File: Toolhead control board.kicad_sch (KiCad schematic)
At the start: 28 parts, among them J1 Conn_01x02_Pin, J2 Conn_01x02_Pin, J3 Conn_01x06_Pin, J4 Conn_01x02_Pin, J5 Conn_01x02_Pin, J6 Conn_01x02_Pin, Q1 AS3400, Q2 AS3400, Q3 AS3400, U1 ADXL345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

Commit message: Rev1. Uart interface
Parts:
- removed J3: Conn_01x06_Pin, Connector_PinHeader_2.54mm:PinHeader_1x06_P2.54mm_Vertical, symbol Connector:Conn_01x06_Pin
- removed R10, R11, R5: OPEN, Resistor_SMD:R_0805_2012Metric, symbol Device:R_US
- added C13: C, Capacitor_SMD:C_0805_2012Metric, symbol Device:C
- added J13: Conn_01x04_Male, Connector_JST:JST_XH_B4B-XH-A_1x04_P2.50mm_Vertical, symbol Connector:Conn_01x04_Male
- added J14: Conn_01x04_Male, Connector_JST:JST_XH_B4B-XH-A_1x04_P2.50mm_Vertical, symbol Connector:Conn_01x03_Pin
- added J3: Conn_01x02_Pin, Connector_JST:JST_XH_S2B-XH-A-1_1x02_P2.50mm_Horizontal, symbol Connector:Conn_01x02_Pin
- added R21, R22, R23, R24, R25: OPEN, Resistor_SMD:R_0805_2012Metric, symbol Device:R_US
- added R6: 22k, Resistor_SMD:R_0805_2012Metric, symbol Device:R_US
- added SW1, SW2: SW_SPST, Button_Switch_SMD:SW_SPST_B3U-1000P, symbol Switch:SW_SPST
- added TP1, TP2, TP3: TestPoint_Probe, TestPoint:TestPoint_Pad_D1.0mm, symbol Connector:TestPoint_Probe
- R3: value 27 -> 4.7k
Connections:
- net +3.3V: now also R3.1, R23.1, R24.1, SW2.1 (A)
- net +5V: now also R21.1
- net +VDC: now also J13.1 (Pin_1), R22.1
- net GND: now also J1.2 (Pin_2), C13.2, J13.4 (Pin_4), J14.1 (Pin_1), J3.2 (Pin_2), R25.2, R6.2, SW1.1 (A); no longer J1.1 (Pin_1)
- net HEATER: now also U2.22 (PA14); no longer U2.15 (PB1)
- net HOTEND_FAN: now also U2.15 (PB1); no longer U2.6 (PA0)
- net PART_FAN: now also U2.21 (PA13); no longer U2.7 (PA1)
- net at J4.1 (Pin_1), J5.1 (Pin_1): now also R12.2, R13.2; no longer Q2.3 (D)
- net RX: now reaches U2.20 (PA10/PA12)
- net RX: now also J13.3 (Pin_3); no longer R3.1
- net ADXL_INT: now reaches U1.8 (INT1)
- net ADXL_INT: now also U2.27 (PB6)
- net at J4.2 (Pin_2): now also J5.2 (Pin_2), Q2.3 (D)
- net at U2.1 (PB8): now also R6.1, SW2.2 (B)
- net PROBE: now reaches U2.28 (PB7)
- net PROBE: now also J14.2 (Pin_2), R24.2, R25.1
- net D+ renamed THERMISTOR_2
- net THERMISTOR_2: now also U2.14 (PB0), C13.1, J3.1 (Pin_1)
- net D- renamed TX
- net TX: now also J13.2 (Pin_2)
- net NRST: no longer names the net of U2.4 (NRST)
- net NRST: now also SW1.2 (B)
- net THERMISTOR renamed THERMISTOR_1
- net THERMISTOR_1: now also J1.1 (Pin_1), U2.6 (PA0); no longer J1.2 (Pin_2), U2.14 (PB0)
- new net: J14.3 (Pin_3), R21.2, R22.2, R23.2
- new net: TP3.1, U2.7 (PA1)
- new net Stepper/INDEX: TP1.1
- new net Stepper/STANDBY: TP2.1
- no-connect marks 5 -> 3
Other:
- sheet Stepper ports: added INDEX, STANDBY; removed none
- note added: "BOOT"
- note added: "PROBE"
- note added: "RESET"
- note added: "SERIAL INTERFACE TO HOST"
- note added: "THERMISTOR 1"
- note added: "THERMISTOR 2"
- note removed: "THERMISTOR"
- moved on the sheet: C1, J1, J4, J5, R1, R2, R7, R9, U1, U2, Y1

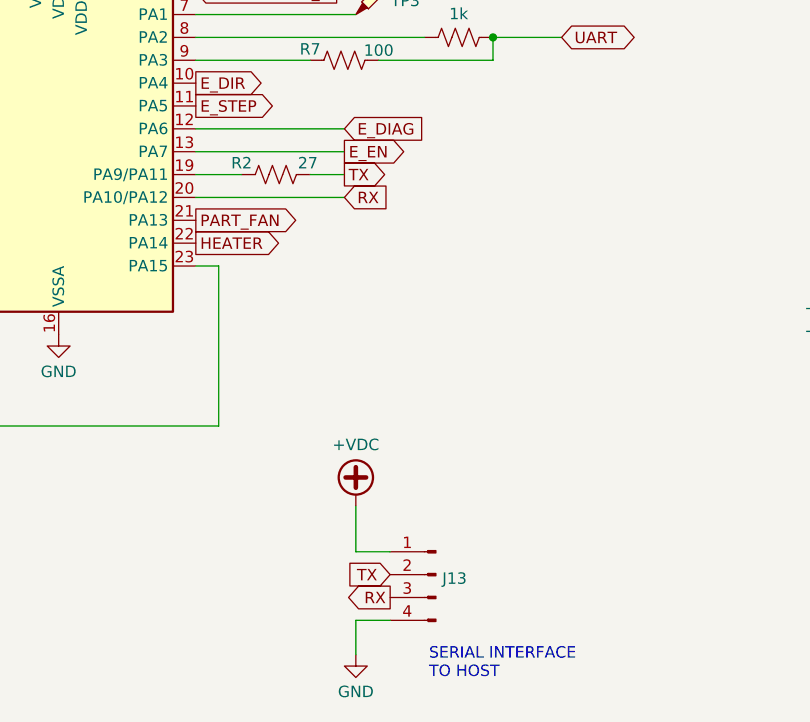
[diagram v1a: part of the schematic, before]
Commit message: Rev2 (USB) largely done
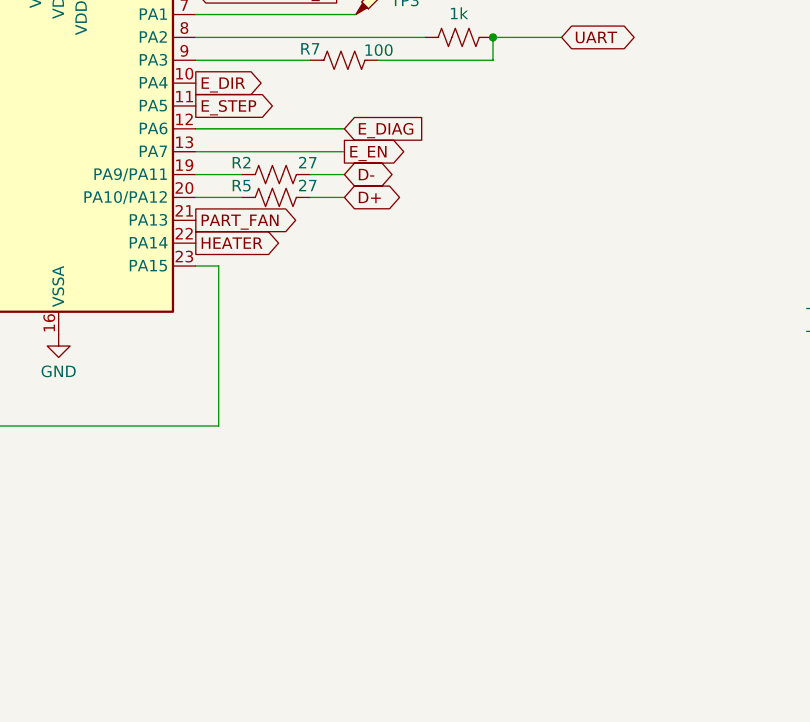
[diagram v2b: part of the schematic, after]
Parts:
- removed J13: Conn_01x04_Male, Connector_JST:JST_XH_B4B-XH-A_1x04_P2.50mm_Vertical, symbol Connector:Conn_01x04_Male
- added R5: 27, Resistor_SMD:R_0805_2012Metric, symbol Device:R_US
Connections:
- net RX: no longer names the net of U2.20 (PA10/PA12)
- net RX: now also R5.1
- net TX renamed D-
- new net D+: R5.2
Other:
- note removed: "SERIAL INTERFACE TO HOST"

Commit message: Rev2, as ordered
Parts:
- J14: footprint Connector_JST:JST_XH_B4B-XH-A_1x04_P2.50mm_Vertical -> Connector_JST:JST_XH_S3B-XH-A-1_1x03_P2.50mm_Horizontal
- R2, R5: footprint Resistor_SMD:R_0805_2012Metric -> Resistor_SMD:R_0603_1608Metric
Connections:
- net +3.3V: no longer U1.6 (Vs)
- net +VDC: now also J2.1 (Pin_1); no longer J2.2 (Pin_2)
- net at Q1.3 (D): now also J2.2 (Pin_2); no longer J2.1 (Pin_1)
- new net +2V5: U1.6 (Vs)
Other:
- moved on the sheet: J2, R6, SW2

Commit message: Rev3 (connectors on back, and with USB daughter board) - probably done
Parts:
- removed R13, R16, R21, R22, R23, R24, R25: OPEN, Resistor_SMD:R_0805_2012Metric, symbol Device:R_US
- added JP11, JP12, JP5, JP6, JP7, JP8, JP9: SolderJumper_2_Open, Jumper:SolderJumper-2_P1.3mm_Open_TrianglePad1.0x1.5mm, symbol Jumper:SolderJumper_2_Open
- added R11: OPEN, Resistor_SMD:R_0603_1608Metric, symbol Device:R_US
- added TP4, TP5: TestPoint_Probe, TestPoint:TestPoint_Pad_D1.0mm, symbol Connector:TestPoint_Probe
- C1, C13: value C -> 0.1uF; footprint Capacitor_SMD:C_0805_2012Metric -> Capacitor_SMD:C_0603_1608Metric
- J1, J3, J4, J5, J6: footprint Connector_JST:JST_XH_S2B-XH-A-1_1x02_P2.50mm_Horizontal -> Connector_JST:JST_XH_B2B-XH-A_1x02_P2.50mm_Vertical
- J2: footprint Connector_JST:JST_XH_S2B-XH-A-1_1x02_P2.50mm_Horizontal -> TerminalBlock_Phoenix:TerminalBlock_Phoenix_PT-1,5-2-3.5-H_1x02_P3.50mm_Horizontal
- R1, R14, R3, R4, R6, R7, R8, R9: footprint Resistor_SMD:R_0805_2012Metric -> Resistor_SMD:R_0603_1608Metric
- R12: footprint Resistor_SMD:R_0805_2012Metric -> Resistor_SMD:R_0603_1608Metric; now not fitted
- R15: value OPEN -> 22k; footprint Resistor_SMD:R_0805_2012Metric -> Resistor_SMD:R_0603_1608Metric
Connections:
- net E_EN is gone; now on net HOTEND_FAN: U2.13 (PA7)
- net +3.3V: now also R12.1, R15.1, JP9.2 (B)
- net +5V: now also JP11.2 (B), JP5.2 (B), JP7.2 (B); no longer R12.1, R15.1
- net +VDC: now also JP12.2 (B), JP6.2 (B), JP8.2 (B)
- net GND: now also R11.2
- net HEATER: now also U2.21 (PA13); no longer U2.22 (PA14)
- net HOTEND_FAN: no longer U2.15 (PB1)
- net PART_FAN: now also U2.22 (PA14); no longer U2.21 (PA13)
- net PROBE: now also R12.2, R11.1
- net THERMISTOR_2: now also U2.15 (PB1); no longer U2.14 (PB0)
- net at J4.1 (Pin_1), J5.1 (Pin_1): now also JP5.1 (A), JP6.1 (A); no longer R12.2
- net at J14.3 (Pin_3): now also JP11.1 (A), JP12.1 (A), JP9.1 (A)
- net at J6.1 (Pin_1): now also JP7.1 (A), JP8.1 (A); no longer R15.2
- net at U1.9 (INT2): now also TP4.1
- net at TP3.1, U2.7 (PA1): now also TP5.1
- new net E_ENN: R15.2, U2.14 (PB0)
- no-connect marks 3 -> 2
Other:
- sheet Stepper ports: added CLK_IN, ENN; removed SHUTDOWN
- moved on the sheet: J14, J2, Q1, R4, R9, TP1, TP2

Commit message: Little changes while populating
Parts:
- added J?: USB_B_Micro, symbol Connector:USB_B_Micro
- J2: footprint TerminalBlock_Phoenix:TerminalBlock_Phoenix_PT-1,5-2-3.5-H_1x02_P3.50mm_Horizontal -> roLib2016:AK550_3.5mm_terminal_block
- SW1, SW2: footprint Button_Switch_SMD:SW_SPST_B3U-1000P -> Button_Switch_SMD:SW_Push_1P1T_NO_CK_KMR2
- U2: value STM32F042G6Ux -> STM32F042G6U6
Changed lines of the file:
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@@
 	)
 	(symbol
+		(lib_id "Connector:USB_B_Micro")
+		(at 95.25 72.39 0)
+		(unit 1)
+		(exclude_from_sim no)
+		(in_bom yes)
+		(on_board yes)
+		(dnp no)
+		(fields_autoplaced yes)
+		(property "Reference" "J?"
+			(at 95.25 60.6255 0)
+			(effects
+				(font
+					(size 1.27 1.27)
+				)
+			)
+		)
+		(property "Value" "USB_B_Micro"
+			(at 95.25 63.0498 0)
+			(effects
+				(font
+					(size 1.27 1.27)
+				)
+			)
+		)
+		(property "Footprint" ""
+			(at 99.06 73.66 0)
+			(effects
+				(font
+					(size 1.27 1.27)
+				)
+				(hide yes)
+			)
+		)
+		(property "Datasheet" "~"
+			(at 99.06 73.66 0)
+			(effects
+				(font
+					(size 1.27 1.27)
+				)
+				(hide yes)
+			)
+		)
+		(property "Description" "USB Micro Type B connector"
+			(at 95.25 72.39 0)
+			(effects
+				(font
+					(size 1.27 1.27)
+				)
+				(hide yes)
+			)
+		)
+		(pin "6"
+		)
+		(pin "5"
+		)
+		(pin "2"
+		)
+		(pin "4"
+		)
+		(pin "1"
+		)
+		(pin "3"
+		)
+		(instances
+			(project ""
+				(path "/c43d474d-039b-4fce-9dd9-f34bcad2a6cb"
+					(reference "J?")
+					(unit 1)
+				)
+			)
+		)
+	)
+	(symbol
 		(lib_id "Connector:Conn_01x03_Pin")
 		(at 77.47 41.91 0)
@@
 			)
 		)
-		(property "Value" "STM32F042G6Ux"
+		(property "Value" "STM32F042G6U6"
 			(at 116.332 98.4363 0)
 			(effects
@@
 			)
 		)
-		(property "Footprint" "TerminalBlock_Phoenix:TerminalBlock_Phoenix_PT-1,5-2-3.5-H_1x02_P3.50mm_Horizontal"
+		(property "Footprint" "roLib2016:AK550_3.5mm_terminal_block"
 			(at 180.34 34.29 0)
 			(effects
@@
 			)
 		)
-		(property "Footprint" "Button_Switch_SMD:SW_SPST_B3U-1000P"
+		(property "Footprint" "Button_Switch_SMD:SW_Push_1P1T_NO_CK_KMR2"
 			(at 81.28 161.29 0)
 			(effects
@@
 			)
 		)
-		(property "Footprint" "Button_Switch_SMD:SW_SPST_B3U-1000P"
+		(property "Footprint" "Button_Switch_SMD:SW_Push_1P1T_NO_CK_KMR2"
 			(at 85.09 92.71 0)
 			(effects

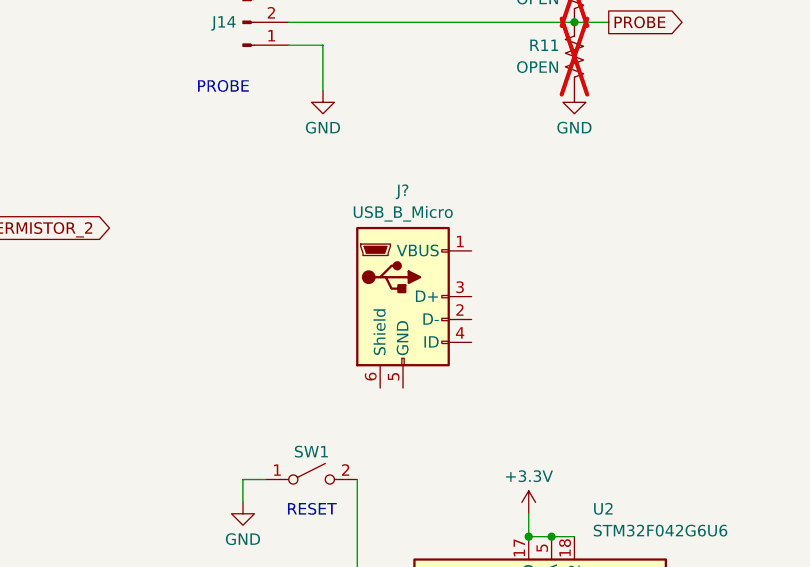
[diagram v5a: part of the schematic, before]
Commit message: Oops I'd saved a test thing accidentally
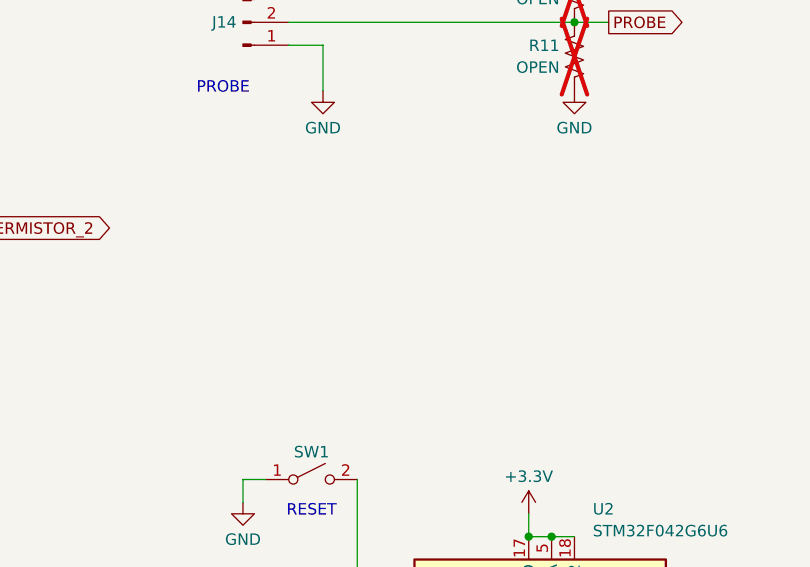
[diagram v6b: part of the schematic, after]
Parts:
- removed J?: USB_B_Micro, symbol Connector:USB_B_Micro
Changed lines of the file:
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@@
-	)
-	(symbol
-		(lib_id "Connector:USB_B_Micro")
-		(at 95.25 72.39 0)
-		(unit 1)
-		(exclude_from_sim no)
-		(in_bom yes)
-		(on_board yes)
-		(dnp no)
-		(fields_autoplaced yes)
-		(property "Reference" "J?"
-			(at 95.25 60.6255 0)
-			(effects
-				(font
-					(size 1.27 1.27)
-				)
-			)
-		)
-		(property "Value" "USB_B_Micro"
-			(at 95.25 63.0498 0)
-			(effects
-				(font
-					(size 1.27 1.27)
-				)
-			)
-		)
-		(property "Footprint" ""
-			(at 99.06 73.66 0)
-			(effects
-				(font
-					(size 1.27 1.27)
-				)
-				(hide yes)
-			)
-		)
-		(property "Datasheet" "~"
-			(at 99.06 73.66 0)
-			(effects
-				(font
-					(size 1.27 1.27)
-				)
-				(hide yes)
-			)
-		)
-		(property "Description" "USB Micro Type B connector"
-			(at 95.25 72.39 0)
-			(effects
-				(font
-					(size 1.27 1.27)
-				)
-				(hide yes)
-			)
-		)
-		(pin "6"
-		)
-		(pin "5"
-		)
-		(pin "2"
-		)
-		(pin "4"
-		)
-		(pin "1"
-		)
-		(pin "3"
-		)
-		(instances
-			(project ""
-				(path "/c43d474d-039b-4fce-9dd9-f34bcad2a6cb"
-					(reference "J?")
-					(unit 1)
-				)
-			)
-		)
 	)
 	(symbol
